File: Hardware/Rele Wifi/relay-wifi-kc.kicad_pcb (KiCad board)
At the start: 2 copper layers, 101.6 x 81 mm, 47 parts, among them J1 SalidaRele1, J2 SalidaRele2, J3 SalidaRele3, J4 SalidaRele4, K1 RELAY_C, K2 RELAY_C, K3 RELAY_C, K4 RELAY_C, Q1 TO23, Q2 TO23, Q3 TO23, Q4 TO23, U1 LM78M05_TO220, U2 ESP32_DevKit_V1_DOIT, U3 PC817, U4 PC817, U5 PC817, U6 PC817

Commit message: Esquematico y PCB V3
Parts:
- D10, D12, D2, D3, D4, D5, D6, D8: footprint Diode_SMD:D_0805_2012Metric_Pad1.15x1.40mm_HandSolder -> Diode_SMD:D_SMA
- moved U1 17.5 mm to (86.4, 96.0)
- moved D5 16.8 mm to (97.0, 96.0), turned to -90 degrees
- moved D13 15.6 mm to (93.8, 45.0)
- moved D11 15.5 mm to (93.7, 62.2)
- moved R9 14.4 mm to (72.6, 32.8), turned to 0 degrees
- moved R7 14.2 mm to (72.6, 50.5), turned to 0 degrees
- moved D4 11.1 mm to (102.1, 96.0), turned to 90 degrees
- moved R6 11.0 mm to (76.2, 86.6)
- moved R8 10.8 mm to (76.2, 69.2)
- moved D3 5.94 mm to (107.2, 96.0), turned to 90 degrees
- moved D9 5.59 mm to (83.8, 77.7)
- moved D7 4.56 mm to (76.2, 100.1)
- moved D2 4.16 mm to (112.3, 96.0), turned to -90 degrees
- moved C1 4.13 mm to (88.3, 103.1)
- moved D8 3.67 mm to (71.4, 63.2), turned to 180 degrees
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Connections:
- C1 pad 2: GND+ -> GND
- C2 pad 2: GND+ -> GND
- D1 pad 1: GND+ -> GND
- D11 pad 1: Net-(D11-K) -> GND
- D13 pad 1: Net-(D13-K) -> GND
- D2 pad 2: GND+ -> GND
- D5 pad 2: GND+ -> GND
- D7 pad 1: Net-(D7-K) -> GND
- D9 pad 1: Net-(D9-K) -> GND
- Q1 pad 2: Net-(D7-A) -> Net-(Q1-B)
- Q1 pad 3: GND+ -> Net-(Q1-E)
- Q2 pad 2: Net-(D11-A) -> Net-(Q2-B)
- Q2 pad 3: GND+ -> Net-(Q2-E)
- Q3 pad 2: Net-(D9-A) -> Net-(Q3-B)
- Q3 pad 3: GND+ -> Net-(Q3-E)
- Q4 pad 2: Net-(D13-A) -> Net-(Q4-B)
- Q4 pad 3: GND+ -> Net-(Q4-E)
- R2 pad 1: Net-(D7-A) -> Net-(Q1-B)
- R3 pad 1: Net-(D9-A) -> Net-(Q3-B)
- R4 pad 1: Net-(D11-A) -> Net-(Q2-B)
- R5 pad 1: Net-(D13-A) -> Net-(Q4-B)
- R6 pad 1: GND+ -> Net-(Q1-E)
- R6 pad 2: Net-(D7-K) -> Net-(D7-A)
- R7 pad 1: GND+ -> Net-(Q2-E)
- R7 pad 2: Net-(D11-K) -> Net-(D11-A)
- R8 pad 1: GND+ -> Net-(Q3-E)
- R8 pad 2: Net-(D9-K) -> Net-(D9-A)
- R9 pad 1: GND+ -> Net-(Q4-E)
- R9 pad 2: Net-(D13-K) -> Net-(D13-A)
- U1 pad 2: GND+ -> GND
- U2 pad 17: GND- -> GND
- U3 pad 2: GND- -> GND
- U3 pad 3: GND+ -> Net-(R2-Pad2)
- U3 pad 4: Net-(R2-Pad2) -> 5V
- U4 pad 2: GND- -> GND
- U4 pad 3: GND+ -> Net-(R3-Pad2)
- U4 pad 4: Net-(R3-Pad2) -> 5V
- U5 pad 2: GND- -> GND
- U5 pad 3: GND+ -> Net-(R4-Pad2)
- U5 pad 4: Net-(R4-Pad2) -> 5V
- U6 pad 2: GND- -> GND
- U6 pad 3: GND+ -> Net-(R5-Pad2)
- U6 pad 4: Net-(R5-Pad2) -> 5V
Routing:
- net 5V: track 194.0 -> 316.7 mm, vias 0 -> 1
- net Net-(Q3-B): track 0.00 -> 17.8 mm
- net Net-(Bronera1-Pin_1): track 10.9 -> 28.6 mm
- net Net-(Q1-B): track 0.00 -> 16.2 mm
- net Net-(Q4-B): track 0.00 -> 15.1 mm
- net Net-(D11-A): track 13.2 -> 28.2 mm, vias 0 -> 1
- net Net-(D13-A): track 13.5 -> 28.1 mm, vias 0 -> 1
- net Net-(Q2-B): track 0.00 -> 13.1 mm
- net Net-(Q3-E): track 0.00 -> 8.01 mm
- net Net-(Q1-E): track 0.00 -> 7.22 mm
- net Net-(D10-A): track 30.2 -> 23.9 mm
- net Net-(R4-Pad2): track 6.06 -> 0.00 mm
- net Net-(D12-A): track 30.2 -> 24.4 mm
- net Net-(D3-K): track 30.6 -> 25.0 mm
- net Net-(Bronera1-Pin_2): track 10.8 -> 16.3 mm
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- added copper zone on B.Cu, net GND
- added copper zone on F.Cu, net GND
- removed copper zone on F.Cu, net GND+
- removed copper zone on B.Cu, net GND-
- removed copper zone on F.Cu, net GND-
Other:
- board size 101.6 x 81 mm -> 101.6 x 81.5 mm
- board text removed: "1. AÑADIR LA PARTE DE LA FUENTE 2. HACER LA MASCARA DE LOS 2 GND 3. COMPRIMIR SI SE PUEDE 4. AÑADIR LOS TEXTOS"

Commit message: Esquematico y PCB V4
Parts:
- moved D1 61.1 mm to (65.9, 97.8)
- moved R1 59.7 mm to (58.3, 96.8), turned to 90 degrees
- moved C2 24.7 mm to (95.8, 85.7), turned to 0 degrees
- moved D13 15.0 mm to (81.8, 35.8)
- moved D11 14.9 mm to (81.8, 53.1)
- moved D7 13.2 mm to (81.8, 88.2)
- moved U1 12.1 mm to (74.3, 96.0)
- moved D9 7.31 mm to (81.8, 70.7)
- moved C1 7.26 mm to (86.9, 96.0), turned to 0 degrees
- moved D10 7.01 mm to (68.1, 52.2), turned to -90 degrees
- moved D12 7.01 mm to (68.1, 34.6), turned to -90 degrees
- moved D6 7.01 mm to (68.1, 87.0), turned to -90 degrees
- moved D8 7.01 mm to (68.1, 69.4), turned to -90 degrees
- moved R7 5.34 mm to (77.9, 49.8)
- moved R9 5.24 mm to (77.9, 32.4)
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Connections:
- net 5V renamed +5V
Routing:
- net +5V: track 316.7 -> 343.8 mm
- net Net-(D11-A): track 28.2 -> 3.26 mm, vias 1 -> 0
- net Net-(D13-A): track 28.1 -> 3.31 mm, vias 1 -> 0
- net Net-(Q3-B): track 17.8 -> 4.84 mm
- net Net-(D8-A): track 27.4 -> 16.3 mm, vias 0 -> 1
- net Net-(Q1-B): track 16.2 -> 5.16 mm
- net Net-(D6-A): track 26.6 -> 15.8 mm, vias 0 -> 1
- net Net-(Q4-B): track 15.1 -> 5.14 mm
- net Net-(D9-A): track 12.3 -> 3.26 mm, vias 1 -> 0
- net Net-(Q2-B): track 13.1 -> 4.73 mm
- net Net-(R4-Pad2): track 0.00 -> 8.28 mm
- net Net-(D12-A): track 24.4 -> 16.5 mm, vias 0 -> 1
- net Net-(D10-A): track 23.9 -> 16.4 mm, vias 0 -> 1
- net Net-(D3-K): track 25.0 -> 31.8 mm
- net Net-(D7-A): track 9.92 -> 3.26 mm, vias 1 -> 0
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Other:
- board size 101.6 x 81.5 mm -> 100.1 x 75.6 mm

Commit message: Esquematico y PCB V5
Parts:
- removed Q4: TO23, Package_TO_SOT_SMD:SOT-23
- added I2C1: Conn_01x04, Connector_PinSocket_2.54mm:PinSocket_1x04_P2.54mm_Vertical, F.Cu at (109.0, 28.2)
- added Q5: BC817, Package_TO_SOT_SMD:SOT-23, F.Cu at (72.3, 69.4)
- Q1, Q2, Q3: value TO23 -> BC817
- moved Q3 34.8 mm to (72.3, 34.6), turned to 180 degrees
- moved Q1 1.51 mm to (72.3, 86.9), turned to 180 degrees
- moved Q2 1.48 mm to (72.3, 52.1), turned to 180 degrees
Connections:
- Q1 pad 1: Net-(D6-A) -> Net-(Q1-B)
- Q1 pad 2: Net-(Q1-B) -> Net-(Q1-E)
- Q1 pad 3: Net-(Q1-E) -> Net-(D6-A)
- Q2 pad 1: Net-(D10-A) -> Net-(Q2-B)
- Q2 pad 2: Net-(Q2-B) -> Net-(Q2-E)
- Q2 pad 3: Net-(Q2-E) -> Net-(D10-A)
- Q3 pad 1: Net-(D8-A) -> Net-(Q3-B)
- Q3 pad 2: Net-(Q3-B) -> Net-(Q3-E)
- Q3 pad 3: Net-(Q3-E) -> Net-(D12-A)
- R10 pad 1: GIPIO27 -> GPIO33
- R11 pad 1: GIPIO26 -> GPIO32
- R12 pad 1: GIPIO33 -> GPIO18
- R13 pad 1: GIPIO32 -> GPIO19
- R3 pad 1: Net-(Q3-B) -> Net-(Q5-B)
- R5 pad 1: Net-(Q4-B) -> Net-(Q3-B)
- R8 pad 1: Net-(Q3-E) -> Net-(Q5-E)
- R9 pad 1: Net-(Q4-E) -> Net-(Q3-E)
- U2 pad 10: GIPIO27 -> unconnected-(U2-IO27-Pad10)
- U2 pad 30: unconnected-(U2-IO18-Pad30) -> GPIO18
- U2 pad 31: unconnected-(U2-IO19-Pad31) -> GPIO19
- U2 pad 32: unconnected-(U2-IO21-Pad32) -> GPIO21
- U2 pad 35: unconnected-(U2-IO22-Pad35) -> GPIO22
- U2 pad 6: GIPIO32 -> GPIO32
- U2 pad 7: GIPIO33 -> GPIO33
- U2 pad 9: GIPIO26 -> unconnected-(U2-IO26-Pad9)
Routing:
- net GPIO18: track 0.00 -> 64.6 mm, vias 0 -> 1
- net GPIO19: track 0.00 -> 48.4 mm, vias 0 -> 1
- net +5V: track 343.8 -> 389.4 mm
- net GPIO33: track 0.00 -> 38.4 mm, vias 0 -> 1
- net GIPIO27: track 30.8 -> 0.00 mm, vias 1 -> 0
- net GPIO21: track 0.00 -> 30.5 mm
- net GPIO32: track 0.00 -> 24.5 mm, vias 0 -> 1
- net GIPIO32: track 21.3 -> 0.00 mm, vias 1 -> 0
- net GPIO22: track 0.00 -> 20.1 mm
- net GIPIO26: track 17.5 -> 0.00 mm, vias 1 -> 0
- net GIPIO33: track 8.32 -> 0.00 mm, vias 1 -> 0
- net Net-(Q4-B): track 5.14 -> 0.00 mm
- net Net-(Q5-E): track 0.00 -> 4.79 mm
- net Net-(Q5-B): track 0.00 -> 4.60 mm
- net Net-(Q4-E): track 3.38 -> 0.00 mm
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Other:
- board size 100.1 x 75.6 mm -> 99.7 x 75.6 mm
- board text added: "I2C"

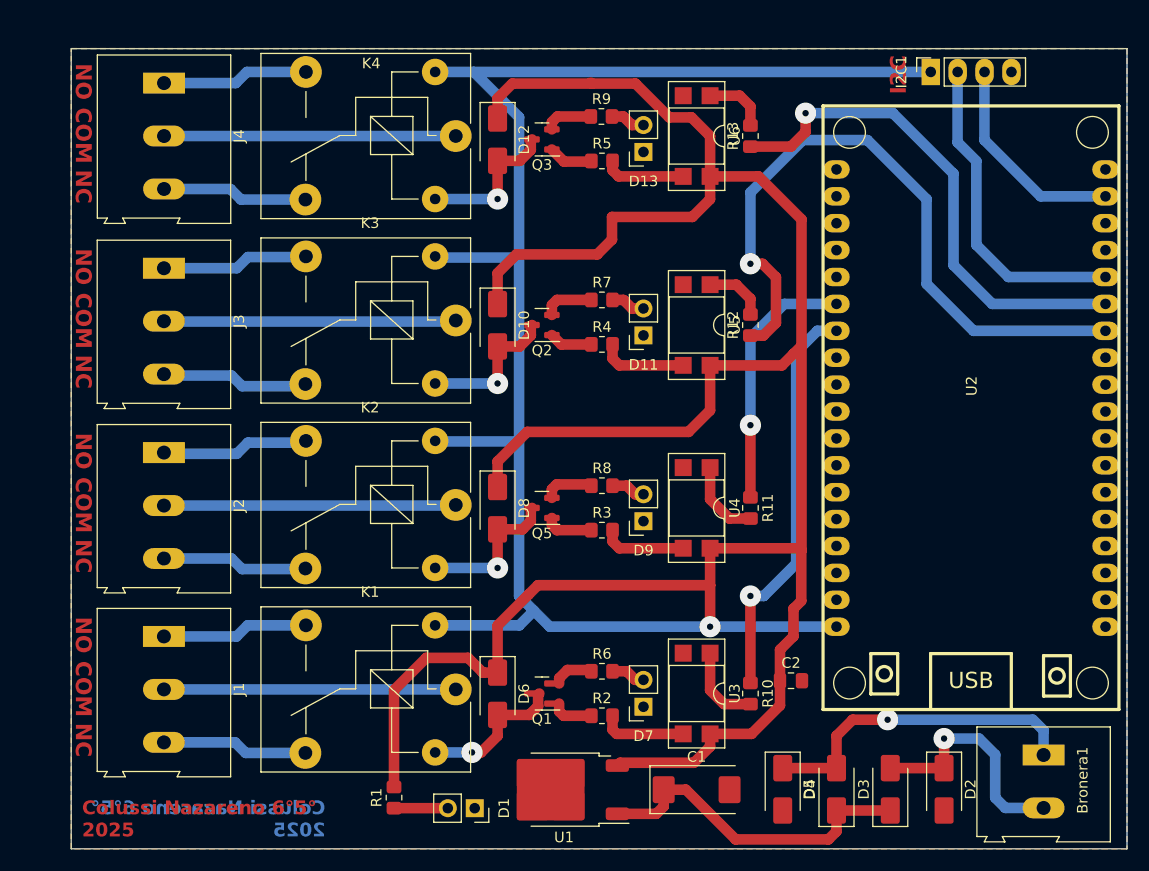
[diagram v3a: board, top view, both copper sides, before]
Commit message: Esquematico y PCB V6
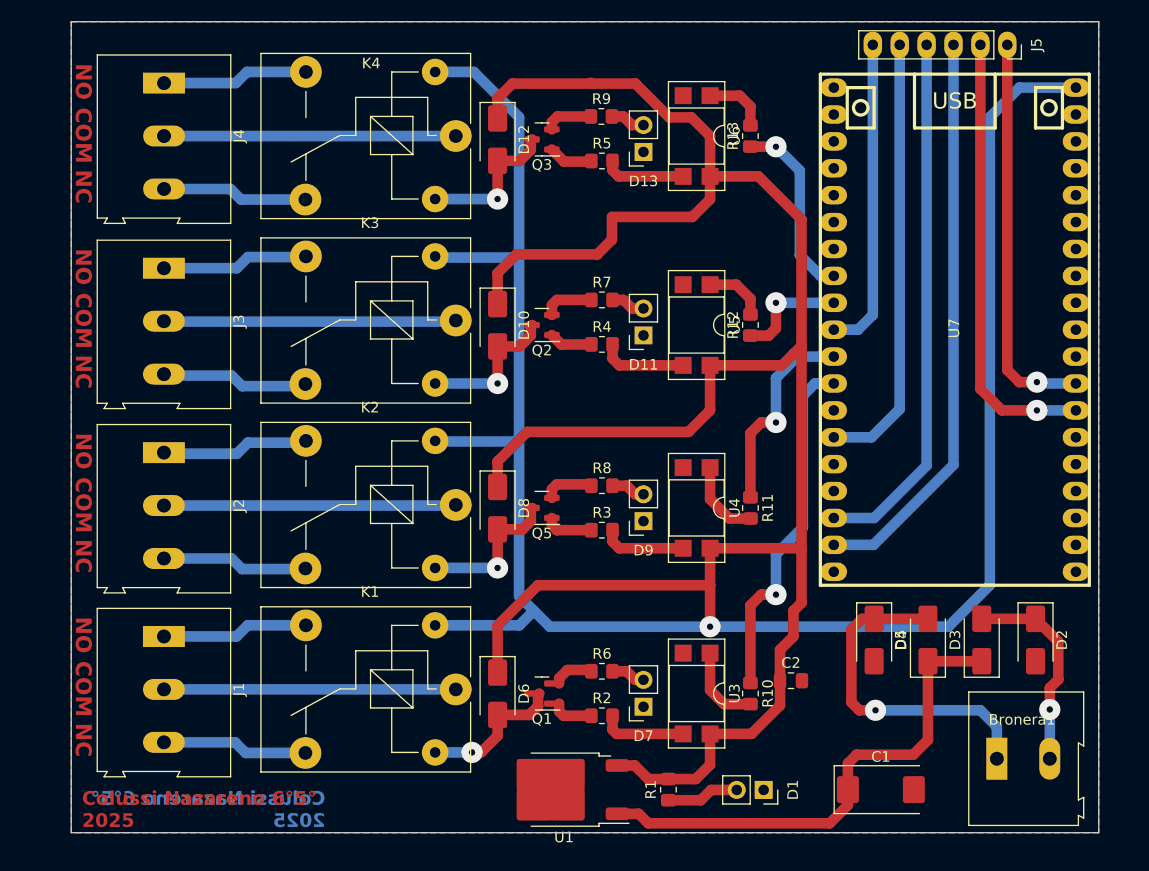
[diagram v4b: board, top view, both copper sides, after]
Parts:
- removed I2C1: Conn_01x04, Connector_PinSocket_2.54mm:PinSocket_1x04_P2.54mm_Vertical
- removed U2: ESP32_DevKit_V1_DOIT, EESTN5:ESP32_DEVKIT_V1_DOIT
- added J5: Conn_01x06, Connector_PinSocket_2.54mm:PinSocket_1x06_P2.54mm_Vertical, F.Cu at (116.2, 25.7)
- added U7: ESP32_DEVKITC, EESTN5:ESP32S, F.Cu at (111.3, 52.6)
- moved D1 27.3 mm to (93.2, 96.0)
- moved R1 25.9 mm to (84.2, 96.0)
- moved C1 17.4 mm to (104.3, 96.0)
- moved D4 16.5 mm to (108.7, 81.9)
- moved D5 16.5 mm to (103.6, 81.9)
- moved D2 16.5 mm to (118.9, 81.9)
- moved D3 16.5 mm to (113.8, 81.9)
- moved Bronera1 4.43 mm to (115.2, 93.1), turned to 0 degrees
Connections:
- R10 pad 1: GPIO33 -> GPIO19
- R11 pad 1: GPIO32 -> GPIO18
- R12 pad 1: GPIO18 -> GPIO17
- R13 pad 1: GPIO19 -> GPIO16
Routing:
- net GPIO23: track 0.00 -> 54.1 mm
- net GPIO18: track 64.6 -> 19.4 mm
- net GPIO22: track 20.1 -> 50.5 mm
- net GPIO5: track 0.00 -> 29.8 mm
- net GPIO32: track 24.5 -> 42.3 mm
- net GPIO16: track 0.00 -> 17.6 mm, vias 0 -> 1
- net Net-(D3-K): track 31.8 -> 47.8 mm
- net GPIO19: track 48.4 -> 33.4 mm
- net GPIO21: track 30.5 -> 41.7 mm
- net GPIO17: track 0.00 -> 10.6 mm, vias 0 -> 1
- net +5V: track 389.4 -> 396.8 mm
- net Net-(Bronera1-Pin_2): track 22.4 -> 19.5 mm
- net Net-(D1-A): track 5.08 -> 6.86 mm
- net Net-(Bronera1-Pin_1): track 31.1 -> 32.2 mm
- net GPIO33: track 38.4 -> 37.7 mm
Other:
- board size 99.7 x 75.6 mm -> 97 x 76.6 mm
- board text removed: "I2C"

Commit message: Esquematico y PCB V7
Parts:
- J5: value Conn_01x06 -> Conn_01x10; footprint Connector_PinSocket_2.54mm:PinSocket_1x06_P2.54mm_Vertical -> Connector_PinSocket_2.54mm:PinSocket_1x10_P2.54mm_Vertical
- moved J5 6.78 mm to (122.9, 24.9)
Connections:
- J5 pad 1: GPIO33 -> GPIO13
- J5 pad 2: GPIO32 -> GPIO27
- J5 pad 3: GPIO23 -> GPIO26
- J5 pad 4: GPIO22 -> GPIO25
- J5 pad 5: GPIO21 -> GPIO33
- J5 pad 6: GPIO5 -> GPIO32
- U7 pad 10: unconnected-(U7-IO26-Pad10) -> GPIO26
- U7 pad 11: unconnected-(U7-IO27-Pad11) -> GPIO27
- U7 pad 15: unconnected-(U7-IO13-Pad15) -> GPIO13
- U7 pad 5: unconnected-(U7-IO34-Pad5) -> GPIO34
- U7 pad 6: unconnected-(U7-IO35-Pad6) -> GPIO35
- U7 pad 9: unconnected-(U7-IO25-Pad9) -> GPIO25
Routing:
- net GPIO23: track 54.1 -> 0.00 mm
- net GPIO34: track 0.00 -> 52.0 mm, vias 0 -> 1
- net GPIO35: track 0.00 -> 48.3 mm, vias 0 -> 1
- net GPIO25: track 0.00 -> 37.8 mm, vias 0 -> 1
- net GPIO26: track 0.00 -> 34.9 mm, vias 0 -> 1
- net GPIO27: track 0.00 -> 30.4 mm, vias 0 -> 1
- net GPIO5: track 29.8 -> 0.00 mm
- net GPIO13: track 0.00 -> 19.3 mm, vias 0 -> 1
- net GPIO33: track 37.7 -> 40.7 mm
- net GPIO32: track 42.3 -> 45.2 mm
- net Net-(Bronera1-Pin_1): track 32.2 -> 33.2 mm
- net GPIO21: track 41.7 -> 41.0 mm
- net GPIO22: track 50.5 -> 51.3 mm
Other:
- board size 97 x 76.6 mm -> 97 x 78.4 mm
- board text added: "13"
- board text added: "22"
- board text added: "23"
- board text added: "25"
- board text added: "26"
- board text added: "27"
- board text added: "32"
- board text added: "33"
- board text added: "34"
- board text added: "35"

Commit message: Esquematico y PCB V8
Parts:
- D11, D13, D7, D9: footprint Connector_PinSocket_2.54mm:PinSocket_1x02_P2.54mm_Vertical -> TerminalBlock_Altech:Altech_AK300_1x02_P5.00mm_45-Degree
- moved U1 24.2 mm to (98.5, 94.9), turned to -90 degrees
- moved D7 16.8 mm to (65.7, 92.5), turned to 0 degrees
- moved D11 14.5 mm to (68.1, 57.6), turned to 0 degrees
- moved D13 14.4 mm to (68.1, 40.1), turned to 0 degrees
- moved D9 14.4 mm to (68.1, 74.9), turned to 0 degrees
- moved R1 9.27 mm to (93.5, 96.0)
- moved R7 4.45 mm to (78.6, 54.2), turned to 180 degrees
- moved R9 4.25 mm to (78.6, 36.6), turned to 180 degrees
- moved R6 4.18 mm to (78.6, 89.0), turned to 180 degrees
- moved R8 4.18 mm to (78.6, 71.4), turned to 180 degrees
- moved R2 4.13 mm to (78.6, 85.0)
- moved R3 4.13 mm to (78.6, 67.4)
- moved R5 4.07 mm to (78.6, 32.6)
- moved R4 3.87 mm to (78.6, 50.2)
- moved D1 2.96 mm to (90.5, 94.8), turned to 0 degrees
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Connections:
- D11 pad 1: GND -> Net-(D10-A)
- D13 pad 1: GND -> Net-(D12-A)
- D7 pad 1: GND -> Net-(D6-A)
- D9 pad 1: GND -> Net-(D8-A)
- Q1 pad 2: Net-(Q1-E) -> GND
- Q2 pad 2: Net-(Q2-E) -> GND
- Q3 pad 2: Net-(Q3-E) -> GND
- Q5 pad 2: Net-(Q5-E) -> GND
- R6 pad 1: Net-(Q1-E) -> +5V
- R7 pad 1: Net-(Q2-E) -> +5V
- R8 pad 1: Net-(Q5-E) -> +5V
- R9 pad 1: Net-(Q3-E) -> +5V
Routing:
- net +5V: track 396.8 -> 426.1 mm
- net Net-(D3-K): track 47.8 -> 25.3 mm
- net Net-(D7-A): track 3.26 -> 9.79 mm
- net Net-(Q2-E): track 4.87 -> 0.00 mm
- net Net-(Q5-E): track 4.79 -> 0.00 mm
- net Net-(Q3-E): track 4.58 -> 0.00 mm
- net Net-(D13-A): track 3.31 -> 7.44 mm
- net Net-(D11-A): track 3.26 -> 7.35 mm
- net GND: track 0.00 -> 4.04 mm, vias 0 -> 4
- net Net-(Q1-E): track 3.91 -> 0.00 mm
- net Net-(D9-A): track 3.26 -> 7.15 mm
- net Net-(D1-A): track 6.86 -> 3.07 mm
- net Net-(R2-Pad2): track 8.15 -> 10.8 mm
- net Net-(Q2-B): track 4.10 -> 6.59 mm
- net Net-(Q3-B): track 4.23 -> 6.66 mm
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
